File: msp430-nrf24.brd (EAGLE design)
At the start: 160 x 100 mm, 12 parts, among them IC1 MSP430G2X53-20N20, IC2 78L33, J1 PWR

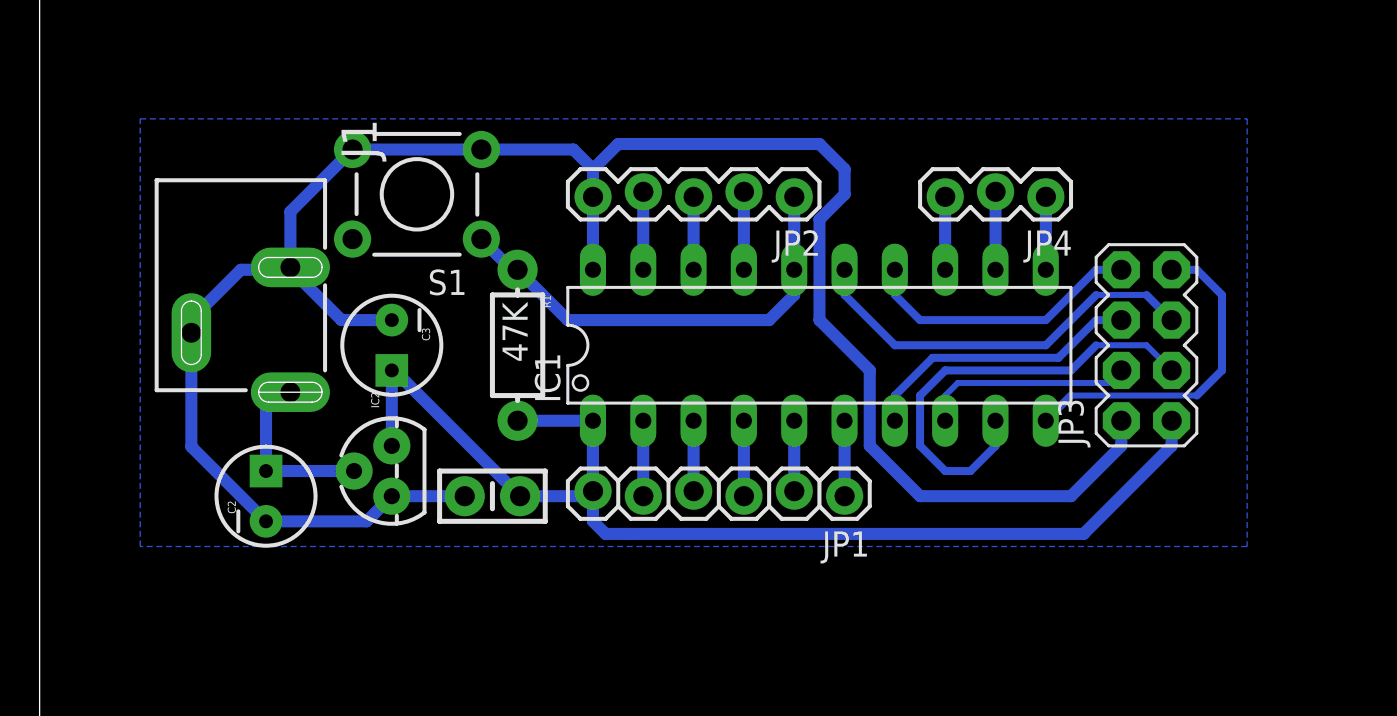
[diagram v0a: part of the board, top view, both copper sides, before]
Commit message: Fixed routing and dc barrel jack
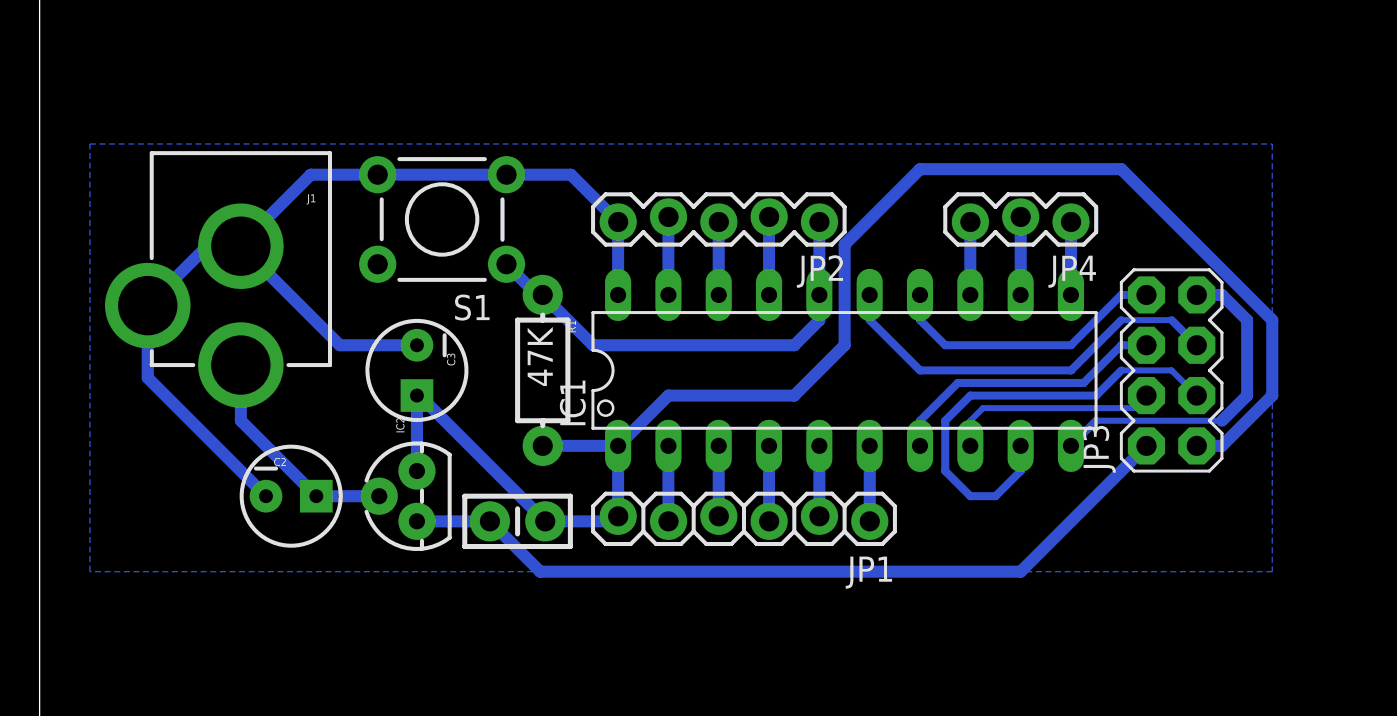
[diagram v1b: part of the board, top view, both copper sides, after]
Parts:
- J1: device SparkFun-Connectors:POWER_JACK_SLOT -> SparkFun-Connectors:POWER_JACK_PTH
- moved J1 5.24 mm to (10.2, 95.2)
- moved C1 1.80 mm to (24.1, 73.7)
- moved JP1 1.80 mm to (41.9, 73.7)
- moved IC1 1.80 mm to (40.6, 81.3)
- moved JP4 1.80 mm to (52.1, 88.9)
- moved C3 1.80 mm to (19.1, 81.3)
- moved IC2 1.80 mm to (19.1, 74.9)
- moved R1 1.80 mm to (25.4, 81.3)
- moved S1 1.80 mm to (20.3, 88.9)
- moved JP2 1.80 mm to (39.4, 88.9)
- moved JP3 1.80 mm to (57.1, 81.3)
- moved C2 1.27 mm to (12.7, 74.9), turned to 0 degrees
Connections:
- net GND: now also J1.GND, J1.GNDBREAK; no longer J1.GND@1, J1.GND@2
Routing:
- net VCC: track 62.0 -> 77.9 mm
- net GND: track 105.1 -> 94.9 mm
- net N$1: track 9.56 -> 11.4 mm

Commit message: Fixed routing
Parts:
- moved C1 1.80 mm to (22.9, 74.9), turned to 270 degrees
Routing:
- net VCC: track 77.9 -> 57.6 mm
- net GND: track 94.9 -> 111.9 mm
- net RST: track 23.0 -> 29.5 mm
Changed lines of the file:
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@@
 </autorouter>
 <elements>
-<element name="C1" library="SparkFun-Capacitors" package="CAP-PTH-SMALL-KIT" value="100nF" x="24.13" y="73.66" rot="R180"/>
+<element name="C1" library="SparkFun-Capacitors" package="CAP-PTH-SMALL-KIT" value="100nF" x="22.86" y="74.93" rot="R270"/>
 <element name="IC1" library="ti_msp430" package="N20" value="MSP430G2X53-20N20" x="40.64" y="81.28"/>
 <element name="JP3" library="SparkFun-Connectors" package="2X4" value="nRF24L01" x="57.15" y="81.28" rot="R90"/>
@@
 <wire x1="39.37" y1="88.773" x2="39.365" y2="88.773" width="0.6096" layer="16"/>
 <wire x1="39.365" y1="88.773" x2="39.365" y2="85.09" width="0.6096" layer="16"/>
-<wire x1="39.365" y1="85.09" x2="39.365" y2="83.815" width="0.6096" layer="16"/>
-<wire x1="39.365" y1="83.815" x2="38.1" y2="82.55" width="0.6096" layer="16"/>
-<wire x1="38.1" y1="82.55" x2="27.94" y2="82.55" width="0.6096" layer="16"/>
-<wire x1="27.94" y1="82.55" x2="25.4" y2="85.09" width="0.6096" layer="16"/>
 <wire x1="25.4" y1="85.09" x2="25.1206" y2="85.09" width="0.6096" layer="16"/>
 <wire x1="25.1206" y1="85.09" x2="23.5712" y2="86.6394" width="0.6096" layer="16"/>
+<wire x1="39.365" y1="85.09" x2="39.365" y2="90.175" width="0.6096" layer="16"/>
+<wire x1="39.365" y1="90.175" x2="38.1" y2="91.44" width="0.6096" layer="16"/>
+<wire x1="38.1" y1="91.44" x2="28.3718" y2="91.44" width="0.6096" layer="16"/>
+<wire x1="28.3718" y1="91.44" x2="23.5712" y2="86.6394" width="0.6096" layer="16"/>
 </signal>
 <signal name="CSN">
@@
 <contactref element="IC2" pad="3"/>
 <contactref element="C3" pad="1"/>
-<wire x1="25.527" y1="73.66" x2="28.956" y2="73.66" width="0.6096" layer="16"/>
 <wire x1="28.956" y1="73.66" x2="29.21" y2="73.914" width="0.6096" layer="16"/>
 <wire x1="19.05" y1="80.01" x2="19.177" y2="80.01" width="0.6096" layer="16"/>
-<wire x1="19.177" y1="80.01" x2="25.527" y2="73.66" width="0.6096" layer="16"/>
 <wire x1="19.05" y1="80.01" x2="19.05" y2="76.2" width="0.6096" layer="16"/>
-<wire x1="58.42" y1="77.47" x2="59.69" y2="77.47" width="0.6096" layer="16"/>
-<wire x1="59.69" y1="77.47" x2="62.23" y2="80.01" width="0.6096" layer="16"/>
-<wire x1="62.23" y1="80.01" x2="62.23" y2="83.82" width="0.6096" layer="16"/>
-<wire x1="62.23" y1="83.82" x2="54.61" y2="91.44" width="0.6096" layer="16"/>
-<wire x1="54.61" y1="91.44" x2="44.45" y2="91.44" width="0.6096" layer="16"/>
-<wire x1="44.45" y1="91.44" x2="40.64" y2="87.63" width="0.6096" layer="16"/>
-<wire x1="40.64" y1="87.63" x2="40.64" y2="82.55" width="0.6096" layer="16"/>
-<wire x1="40.64" y1="82.55" x2="38.1" y2="80.01" width="0.6096" layer="16"/>
-<wire x1="38.1" y1="80.01" x2="31.745" y2="80.01" width="0.6096" layer="16"/>
-<wire x1="31.745" y1="80.01" x2="29.205" y2="77.47" width="0.6096" layer="16"/>
+<wire x1="29.205" y1="77.47" x2="29.205" y2="72.395" width="0.6096" layer="16"/>
+<wire x1="29.205" y1="72.395" x2="30.48" y2="71.12" width="0.6096" layer="16"/>
+<wire x1="30.48" y1="71.12" x2="52.07" y2="71.12" width="0.6096" layer="16"/>
+<wire x1="52.07" y1="71.12" x2="58.42" y2="77.47" width="0.6096" layer="16"/>
+<wire x1="19.177" y1="80.01" x2="22.86" y2="76.327" width="0.6096" layer="16"/>
+<wire x1="22.86" y1="76.327" x2="24.257" y2="76.327" width="0.6096" layer="16"/>
+<wire x1="24.257" y1="76.327" x2="25.4" y2="77.47" width="0.6096" layer="16"/>
 </signal>
 <signal name="GND">
@@
 <contactref element="S1" pad="4"/>
 <contactref element="JP2" pad="5"/>
-<wire x1="29.21" y1="88.773" x2="29.205" y2="88.773" width="0.6096" layer="16"/>
-<wire x1="29.205" y1="88.773" x2="29.205" y2="85.09" width="0.6096" layer="16"/>
 <wire x1="29.083" y1="88.9" x2="29.21" y2="88.773" width="0.6096" layer="16"/>
 <contactref element="IC2" pad="1"/>
@@
 <vertex x="2.54" y="71.12"/>
 </polygon>
-<wire x1="22.733" y1="73.66" x2="19.05" y2="73.66" width="0.6096" layer="16"/>
 <wire x1="19.05" y1="82.55" x2="15.16" y2="82.55" width="0.6096" layer="16"/>
 <wire x1="15.16" y1="82.55" x2="10.16" y2="87.55" width="0.6096" layer="16"/>
@@
 <wire x1="10.16" y1="87.63" x2="8.54" y2="87.63" width="0.6096" layer="16"/>
 <wire x1="8.54" y1="87.63" x2="5.46" y2="84.55" width="0.6096" layer="16"/>
-<wire x1="23.5712" y1="91.1606" x2="26.8224" y2="91.1606" width="0.6096" layer="16"/>
-<wire x1="26.8224" y1="91.1606" x2="29.21" y2="88.773" width="0.6096" layer="16"/>
-<wire x1="55.88" y1="77.47" x2="49.53" y2="71.12" width="0.6096" layer="16"/>
-<wire x1="49.53" y1="71.12" x2="25.273" y2="71.12" width="0.6096" layer="16"/>
-<wire x1="25.273" y1="71.12" x2="22.733" y2="73.66" width="0.6096" layer="16"/>
 <wire x1="5.46" y1="84.55" x2="5.46" y2="80.9" width="0.6096" layer="16"/>
 <wire x1="5.46" y1="80.9" x2="11.43" y2="74.93" width="0.6096" layer="16"/>
+<wire x1="55.88" y1="77.47" x2="52.07" y2="73.66" width="0.6096" layer="16"/>
+<wire x1="52.07" y1="73.66" x2="45.72" y2="73.66" width="0.6096" layer="16"/>
+<wire x1="45.72" y1="73.66" x2="43.18" y2="76.2" width="0.6096" layer="16"/>
+<wire x1="43.18" y1="76.2" x2="43.18" y2="78.74" width="0.6096" layer="16"/>
+<wire x1="43.18" y1="78.74" x2="40.64" y2="81.28" width="0.6096" layer="16"/>
+<wire x1="40.64" y1="81.28" x2="29.21" y2="81.28" width="0.6096" layer="16"/>
+<wire x1="29.21" y1="81.28" x2="21.59" y2="81.28" width="0.6096" layer="16"/>
+<wire x1="21.59" y1="81.28" x2="20.32" y2="82.55" width="0.6096" layer="16"/>
+<wire x1="20.32" y1="82.55" x2="19.05" y2="82.55" width="0.6096" layer="16"/>
+<wire x1="29.21" y1="88.773" x2="29.21" y2="81.28" width="0.6096" layer="16"/>
+<wire x1="29.21" y1="88.773" x2="29.21" y2="85.095" width="0.6096" layer="16"/>
+<wire x1="29.21" y1="85.095" x2="29.205" y2="85.09" width="0.6096" layer="16"/>
+<wire x1="22.86" y1="73.533" x2="19.05" y2="73.533" width="0.6096" layer="16"/>
+<wire x1="19.05" y1="73.533" x2="16.383" y2="73.533" width="0.6096" layer="16"/>
+<wire x1="16.383" y1="73.533" x2="15.24" y2="72.39" width="0.6096" layer="16"/>
+<wire x1="15.24" y1="72.39" x2="13.97" y2="72.39" width="0.6096" layer="16"/>
+<wire x1="13.97" y1="72.39" x2="11.43" y2="74.93" width="0.6096" layer="16"/>
+<wire x1="19.05" y1="73.66" x2="19.05" y2="73.533" width="0.6096" layer="16"/>
 </signal>
 <signal name="P1.0">

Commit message: :new: Change board layout
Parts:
- removed JP1: H1, SparkFun-Connectors:1X06_LOCK
- removed JP2: H2, SparkFun-Connectors:1X05_LOCK
- removed JP3: nRF24L01, SparkFun-Connectors:2X4
- removed JP4: H3, SparkFun-Connectors:1X03_LOCK
- added SV1: (no value), con-lstb:MA03-1
- added SV2: (no value), con-lstb:MA05-1
- added SV3: (no value), con-lstb:MA06-1
- added SV4: (no value), con-lstb:MA04-2
- moved J1 82.3 mm to (-3.05, 14.0), turned to 270 degrees
- moved R1 74.5 mm to (18.3, 7.11)
- moved S1 72.2 mm to (17.5, 16.8)
- moved C3 71.8 mm to (14.0, 9.65)
- moved C1 71.6 mm to (15.0, 3.81)
- moved C2 71.6 mm to (4.83, 3.81)
- moved IC2 71.6 mm to (11.2, 3.81)
- moved IC1 71.4 mm to (34.5, 10.2)
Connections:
- net CE: now also SV4.5; no longer JP3.4
- net CSN: now also SV4.6; no longer JP3.3
- net GND: now also SV2.5, SV4.7; no longer JP2.5, JP3.2
- net IRQ: now also SV4.2; no longer JP3.7
- net MISO: now also SV4.1; no longer JP3.8
- net MOSI: now also SV4.4; no longer JP3.5
- net P1.0: now also SV3.5; no longer JP1.5
- net P1.1: now also SV3.4; no longer JP1.4
- net P1.2: now also SV3.3; no longer JP1.3
- net P1.3: now also SV3.2; no longer JP1.2
- net P1.4: now also SV3.1; no longer JP1.1
- net P2.3: now also SV1.1; no longer JP4.1
- net P2.4: now also SV1.2; no longer JP4.2
- net P2.5: now also SV1.3; no longer JP4.3
- net P2.6: now also SV2.4; no longer JP2.4
- net P2.7: now also SV2.3; no longer JP2.3
- net RST: now also SV2.1; no longer JP2.1
- net SCK: now also SV4.3; no longer JP3.6
- net TEST: now also SV2.2; no longer JP2.2
- net VCC: now also SV3.6, SV4.8; no longer JP1.6, JP3.1
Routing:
- net MOSI: track 20.4 -> 27.1 mm
- net RST: track 29.5 -> 23.3 mm
- net MISO: track 14.3 -> 19.7 mm
- net VCC: track 57.6 -> 53.4 mm
- net GND: track 111.9 -> 108.2 mm
- net N$1: track 11.4 -> 14.0 mm
- net IRQ: track 16.8 -> 14.6 mm
- net CSN: track 24.2 -> 22.5 mm
- net P1.1: track 4.07 -> 3.05 mm
- net P2.4: track 3.94 -> 3.05 mm
- net P2.6: track 3.94 -> 3.05 mm
- net TEST: track 3.94 -> 3.05 mm
- net P1.0: track 3.82 -> 3.05 mm
- net P1.4: track 3.81 -> 3.05 mm
- net P1.2: track 3.81 -> 3.05 mm
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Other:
- board size 160 x 100 mm -> 54.1 x 21.5 mm
